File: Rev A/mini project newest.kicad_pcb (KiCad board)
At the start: 2 copper layers, 82.5 x 63.5 mm, 19 parts, among them J1 Conn_01x01, Q1 Q_NMOS_DSG, U1 ICM7555xB, U2 ICM7555xB

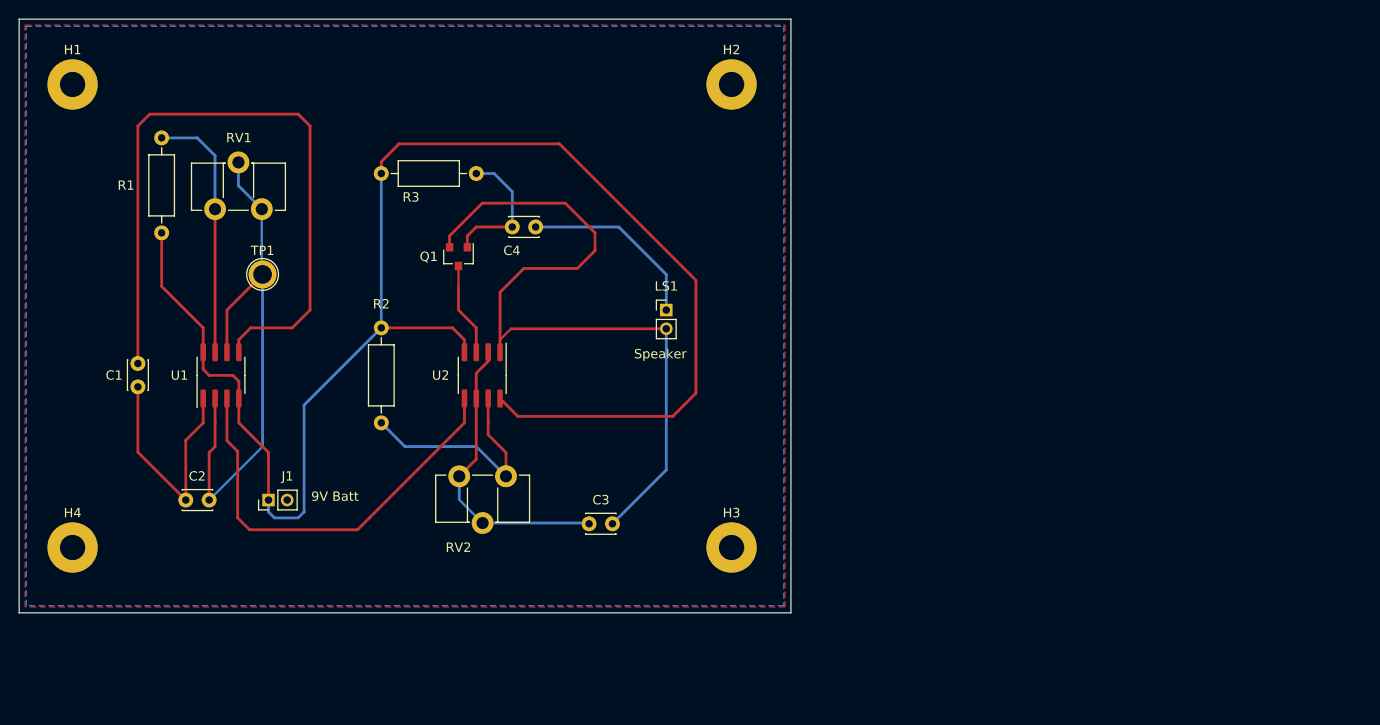
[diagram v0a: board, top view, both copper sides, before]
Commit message: new foot prints, new traces, new coat of paint. a few errors still need to be worked out, mostly with footprints not playing well with thicc traces
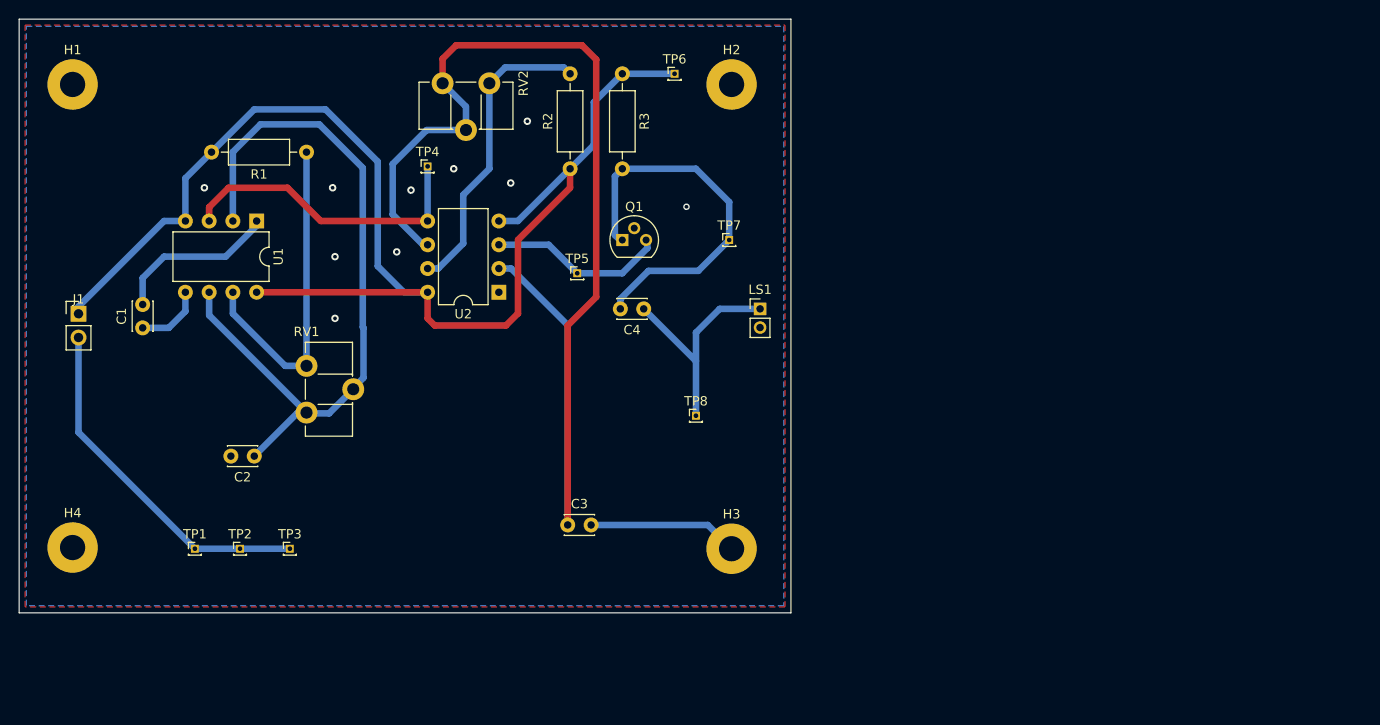
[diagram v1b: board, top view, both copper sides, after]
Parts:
- added TP2: TestPoint, Connector_PinHeader_1.00mm:PinHeader_1x01_P1.00mm_Vertical, F.Cu at (68.1, 113.8)
- added TP3: TestPoint, Connector_PinHeader_1.00mm:PinHeader_1x01_P1.00mm_Vertical, F.Cu at (73.4, 113.8)
- added TP4: TestPoint, Connector_PinHeader_1.00mm:PinHeader_1x01_P1.00mm_Vertical, F.Cu at (88.1, 72.9)
- added TP5: TestPoint, Connector_PinHeader_1.00mm:PinHeader_1x01_P1.00mm_Vertical, F.Cu at (104.1, 84.3)
- added TP6: TestPoint, Connector_PinHeader_1.00mm:PinHeader_1x01_P1.00mm_Vertical, F.Cu at (114.6, 63.0)
- added TP7: TestPoint, Connector_PinHeader_1.00mm:PinHeader_1x01_P1.00mm_Vertical, F.Cu at (120.4, 80.8)
- added TP8: TestPoint, Connector_PinHeader_1.00mm:PinHeader_1x01_P1.00mm_Vertical, F.Cu at (116.8, 99.6)
- J1: value Conn_01x01 -> Conn_01x02; footprint Connector_PinHeader_2.00mm:PinHeader_1x02_P2.00mm_Vertical -> Connector_PinHeader_2.54mm:PinHeader_1x02_P2.54mm_Vertical
- Q1: footprint Package_TO_SOT_SMD:SOT-23 -> Package_TO_SOT_THT:TO-92
- TP1: footprint TestPoint:TestPoint_Plated_Hole_D2.0mm -> Connector_PinHeader_1.00mm:PinHeader_1x01_P1.00mm_Vertical
- U1, U2: value ICM7555xB -> LM555; footprint Package_SO:SOIC-8_3.9x4.9mm_P1.27mm -> Package_DIP:DIP-8_W7.62mm
- moved RV2 42.1 mm to (94.7, 64.0)
- moved TP1 30.2 mm to (63.2, 113.8)
- moved J1 28.5 mm to (50.8, 88.7), turned to 0 degrees
- moved R3 27.9 mm to (109.0, 63.0), turned to 270 degrees
- moved R2 26.4 mm to (103.4, 73.2), turned to 90 degrees
- moved RV1 19.4 mm to (75.2, 94.2), turned to 0 degrees
- moved Q1 17.6 mm to (109.0, 80.8), turned to 0 degrees
- moved U1 16.9 mm to (69.8, 78.7), turned to 270 degrees
- moved R1 15.6 mm to (75.2, 71.4), turned to 180 degrees
- moved C4 14.5 mm to (111.3, 88.1)
- moved LS1 10.0 mm to (123.7, 88.1)
- moved U2 9.07 mm to (95.8, 86.4), turned to 180 degrees
- moved C2 6.74 mm to (69.6, 103.9)
- moved C1 3.84 mm to (57.7, 90.2), turned to 90 degrees
- moved C3 2.29 mm to (103.1, 111.3)
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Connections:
- J1 pad 2: (no net) -> GND
- TP1 pad 1: Net-(C2-Pad1) -> GND
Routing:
- net Net-(C3-Pad1): track 32.0 -> 128.4 mm
- net Earth: track 107.2 -> 34.0 mm, vias 0 -> 10
- net Net-(C1-Pad1): track 74.8 -> 7.34 mm
- net GND: track 0.00 -> 37.9 mm
- net +9V: track 168.5 -> 141.6 mm
- net Net-(C4-Pad2): track 14.8 -> 40.6 mm
- net Net-(C2-Pad1): track 60.6 -> 79.4 mm
- net Net-(TP4-Pad1): track 45.4 -> 33.0 mm
- net Net-(Q1-Pad3): track 10.0 -> 19.0 mm
- net Net-(R2-Pad2): track 24.8 -> 32.8 mm
- net Net-(R1-Pad1): track 27.5 -> 35.3 mm
- net Net-(C4-Pad1): track 19.9 -> 24.7 mm
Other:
- net class Analog: clearance 0.2 -> 0.89916; trace_width 0.3 -> 0.70104; via_dia 0.8 -> 0.70104
- board text removed: "9V Batt"
- board text removed: "Speaker"

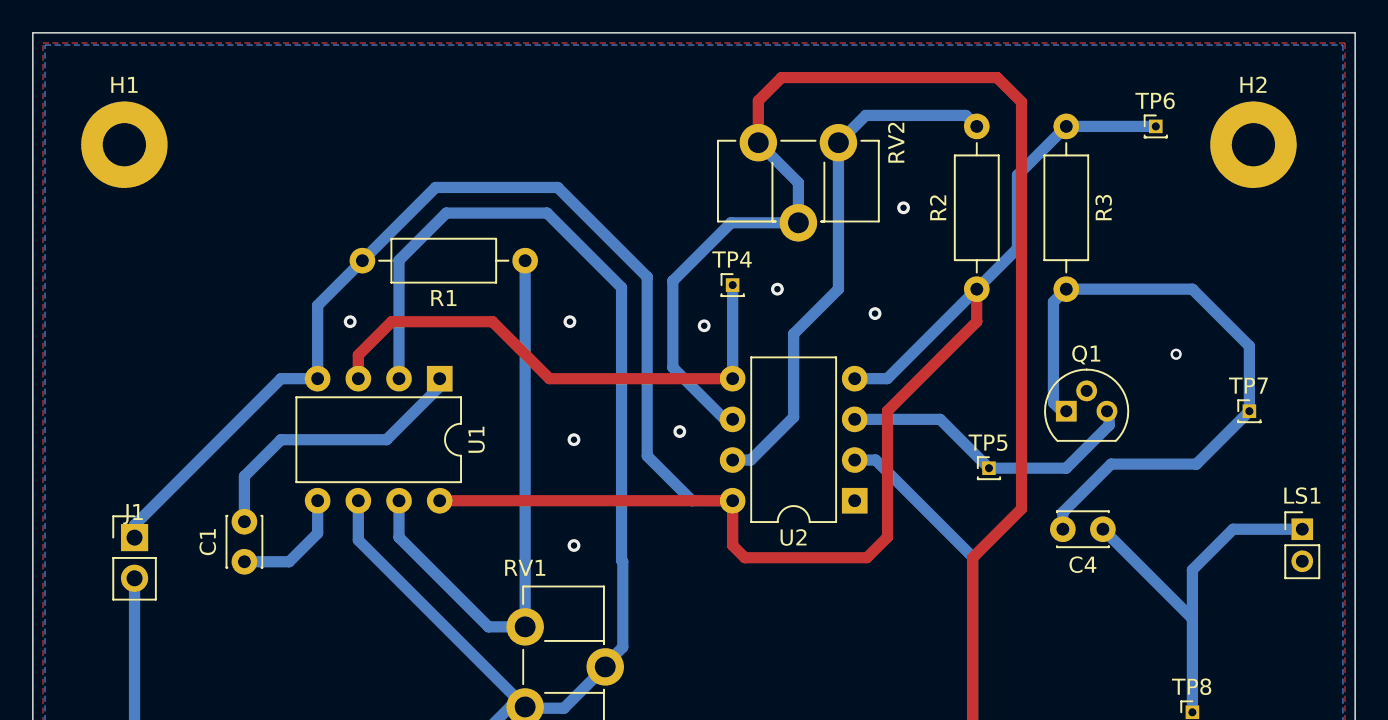
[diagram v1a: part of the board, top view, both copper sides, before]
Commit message: fixed mosfet footprint, made vias bigger, going to clean up traces
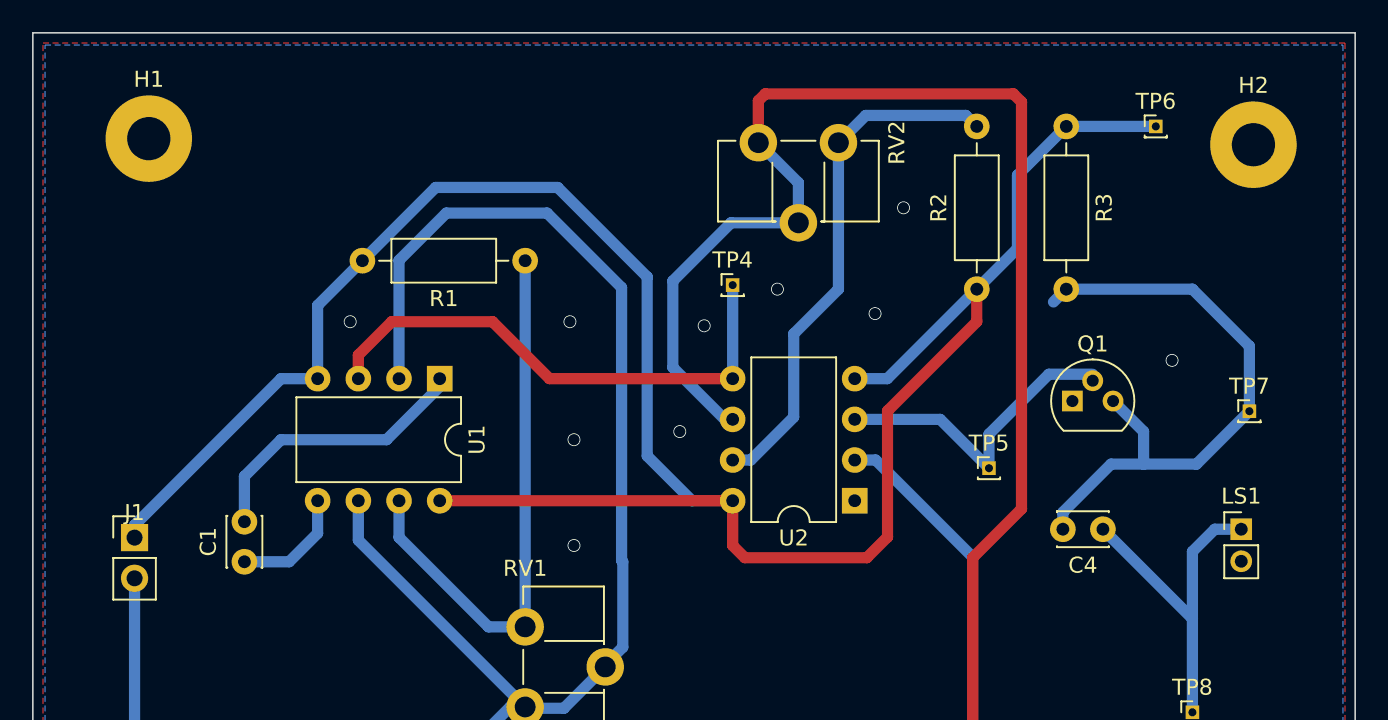
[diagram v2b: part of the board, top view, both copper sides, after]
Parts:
- Q1: value Q_NMOS_DSG -> Q_NMOS_SGD
- moved LS1 3.81 mm to (119.9, 88.1)
- moved H1 1.57 mm to (51.7, 63.8)
- moved Q1 0.74 mm to (109.3, 80.1)
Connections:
- Q1 pad 1: Net-(C4-Pad2) -> Earth
- Q1 pad 2: Earth -> Net-(Q1-Pad2)
- Q1 pad 3: Net-(Q1-Pad3) -> Net-(C4-Pad2)
- TP5 pad 1: Net-(Q1-Pad3) -> Net-(Q1-Pad2)
- U2 pad 3: Net-(Q1-Pad3) -> Net-(Q1-Pad2)
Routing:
- net Net-(Q1-Pad2): track 0.00 -> 19.8 mm
- net Net-(Q1-Pad3): track 19.0 -> 0.00 mm
- net Net-(C4-Pad1): track 24.7 -> 21.6 mm
- net Net-(C4-Pad2): track 40.6 -> 37.9 mm
- net Net-(C3-Pad1): track 128.4 -> 127.6 mm
- net Earth: vias 10 -> 9
- net (no net): vias 0 -> 1
